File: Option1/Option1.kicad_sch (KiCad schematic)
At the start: 0 parts

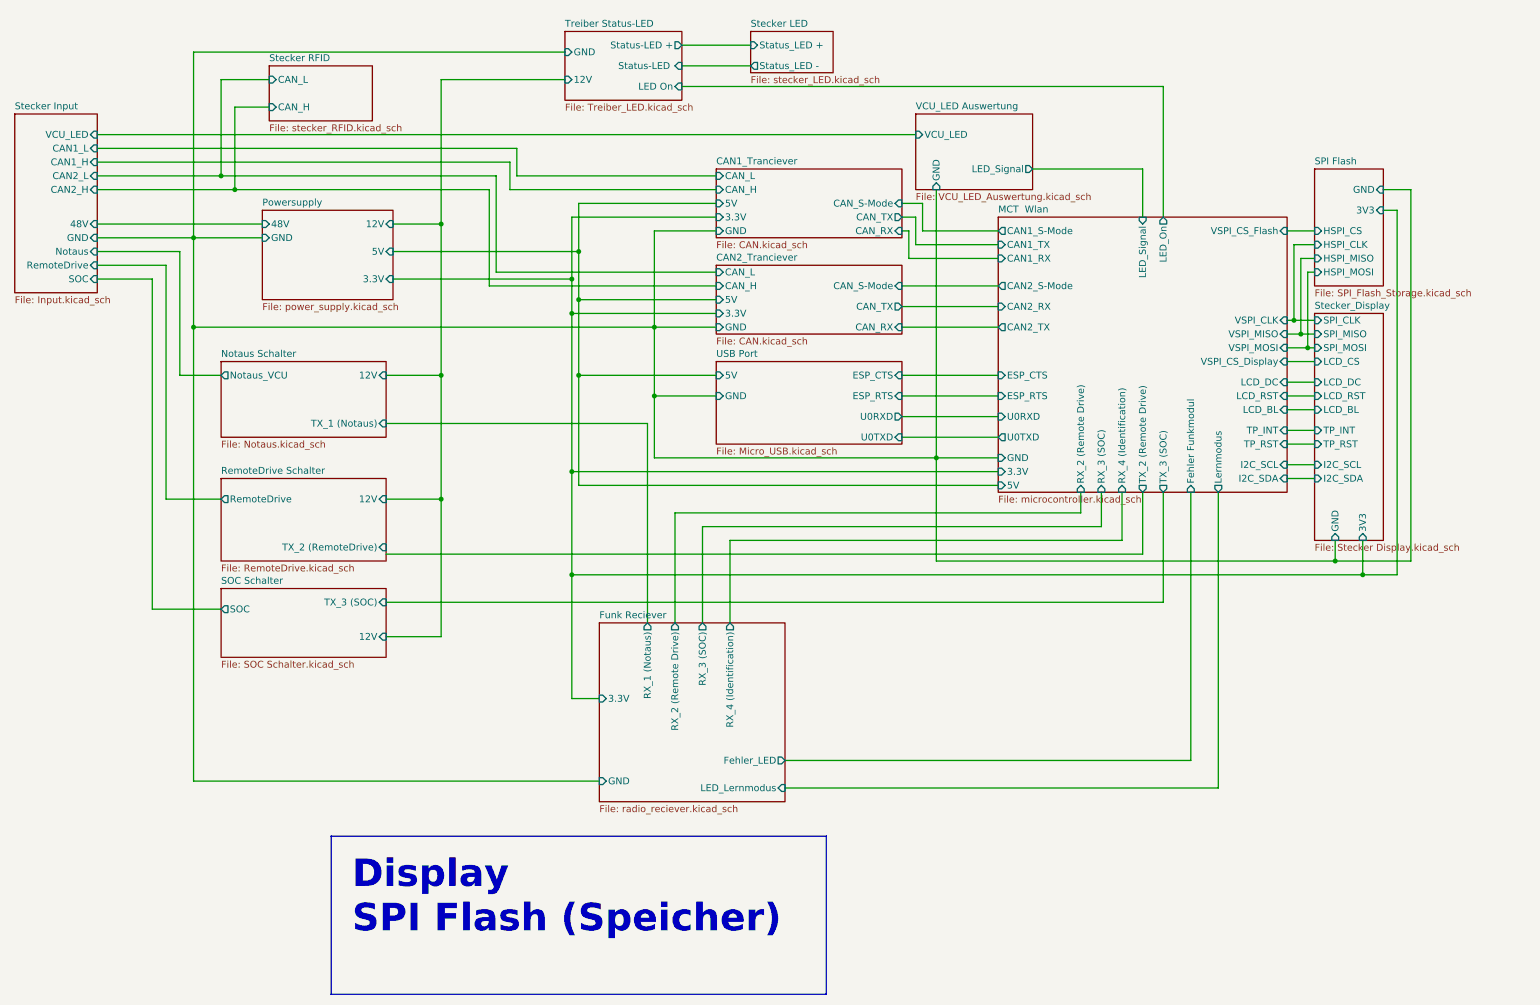
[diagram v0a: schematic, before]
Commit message: SPI Flash hinzugefügt, IN/Outputs vereinheitlicht, USB Flash Möglichkeit hinzugefügt, Display fehtl noch
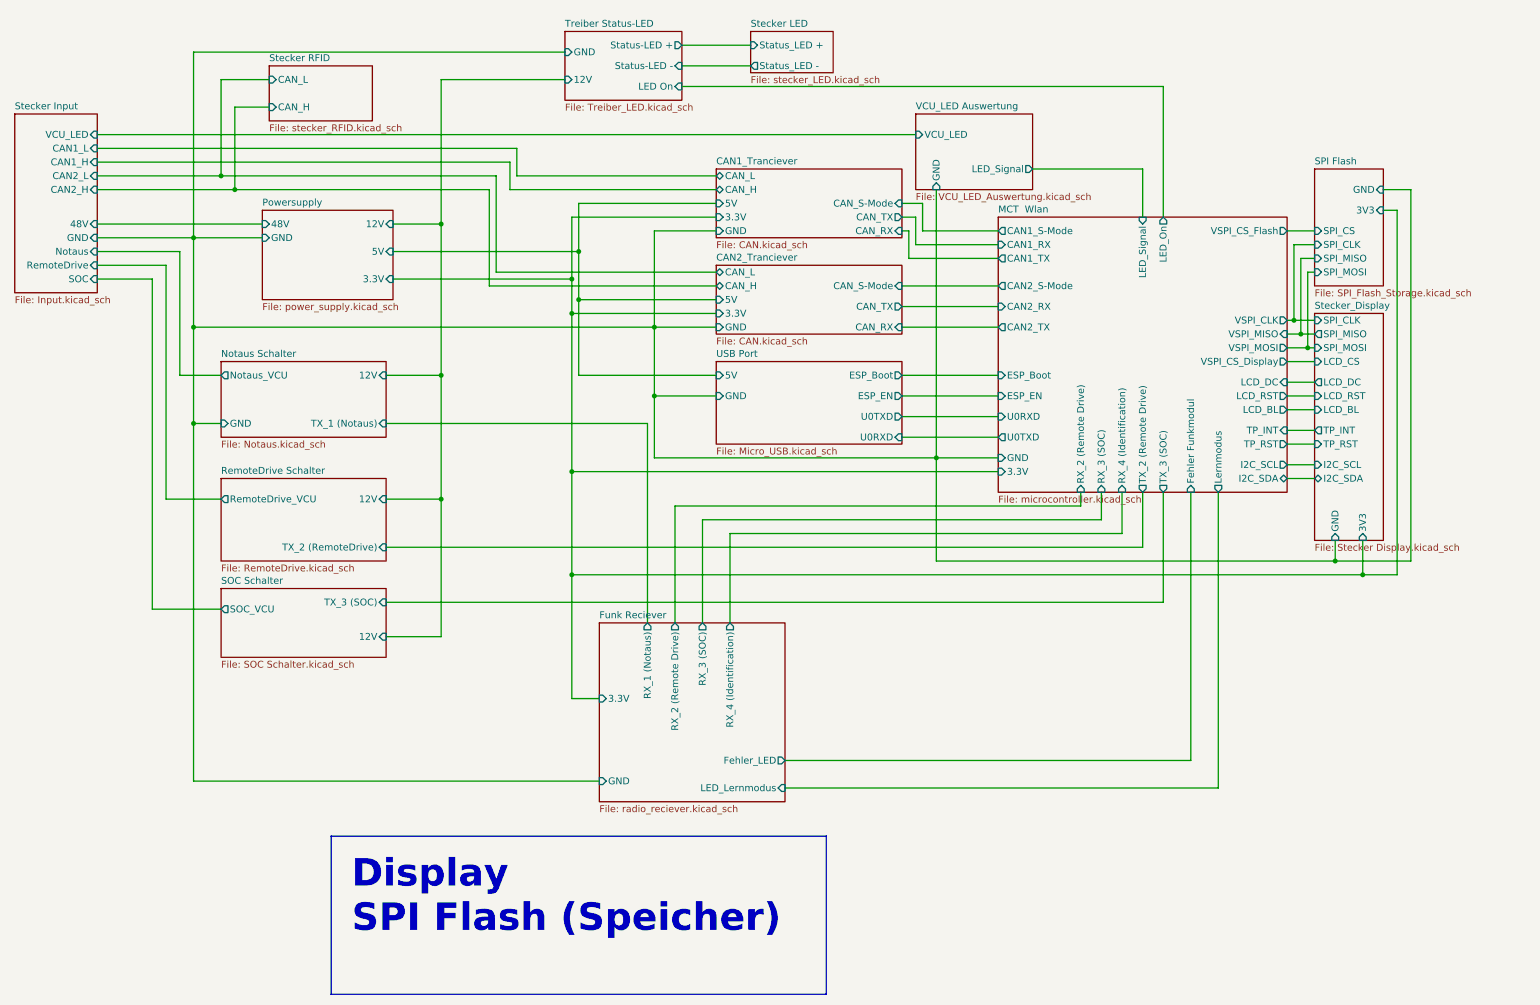
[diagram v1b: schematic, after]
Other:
- sheet MCT  Wlan ports: added ESP_Boot, ESP_EN; removed 5V, ESP_CTS, ESP_RTS
- sheet Notaus Schalter ports: added GND; removed none
- sheet RemoteDrive Schalter ports: added RemoteDrive_VCU; removed RemoteDrive
- sheet SOC Schalter ports: added SOC_VCU; removed SOC
- sheet SPI Flash ports: added SPI_CLK, SPI_CS, SPI_MISO, SPI_MOSI; removed HSPI_CLK, HSPI_CS, HSPI_MISO, HSPI_MOSI
- sheet Treiber Status-LED ports: added Status-LED -; removed Status-LED 
- sheet USB Port ports: added ESP_Boot, ESP_EN; removed ESP_CTS, ESP_RTS

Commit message: Added Export for Review 1
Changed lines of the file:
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@@
 		(comment 3 "Sebastian Hampl")
-	)
-	(text_box "Display\nSPI Flash (Speicher)\n"
-		(exclude_from_sim no)
-		(at 82.55 166.37 0)
-		(size 91.44 29.21)
-		(margins 3.81 3.81 3.81 3.81)
-		(stroke
-			(width 0)
-			(type default)
-		)
-		(fill
-			(type none)
-		)
-		(effects
-			(font
-				(size 5.08 5.08)
-				(thickness 1.016)
-				(bold yes)
-			)
-			(justify left top)
-		)
 	)
 	(junction

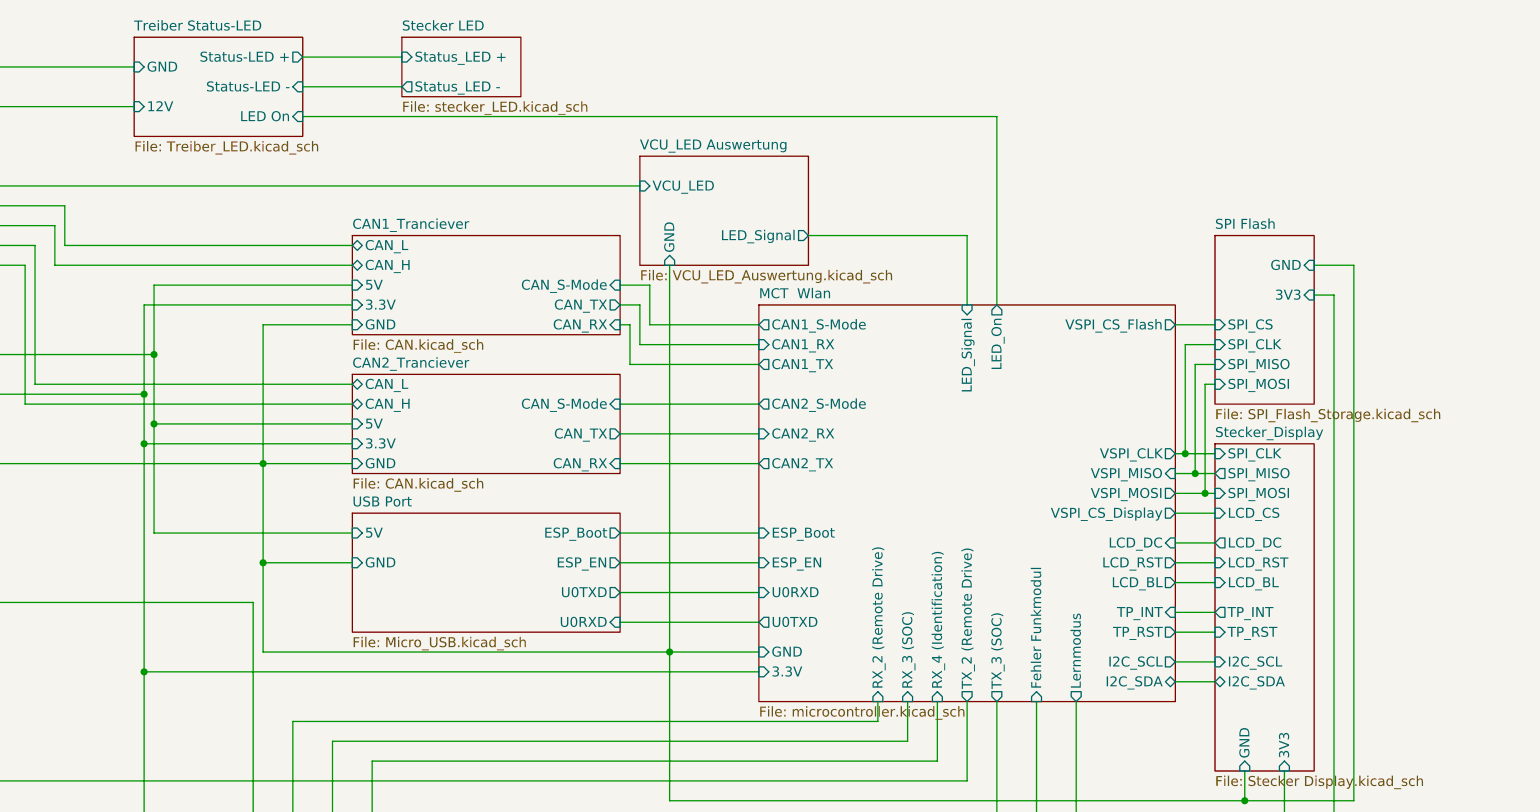
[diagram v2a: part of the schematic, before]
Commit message: USB auf 3V3 umgebaut
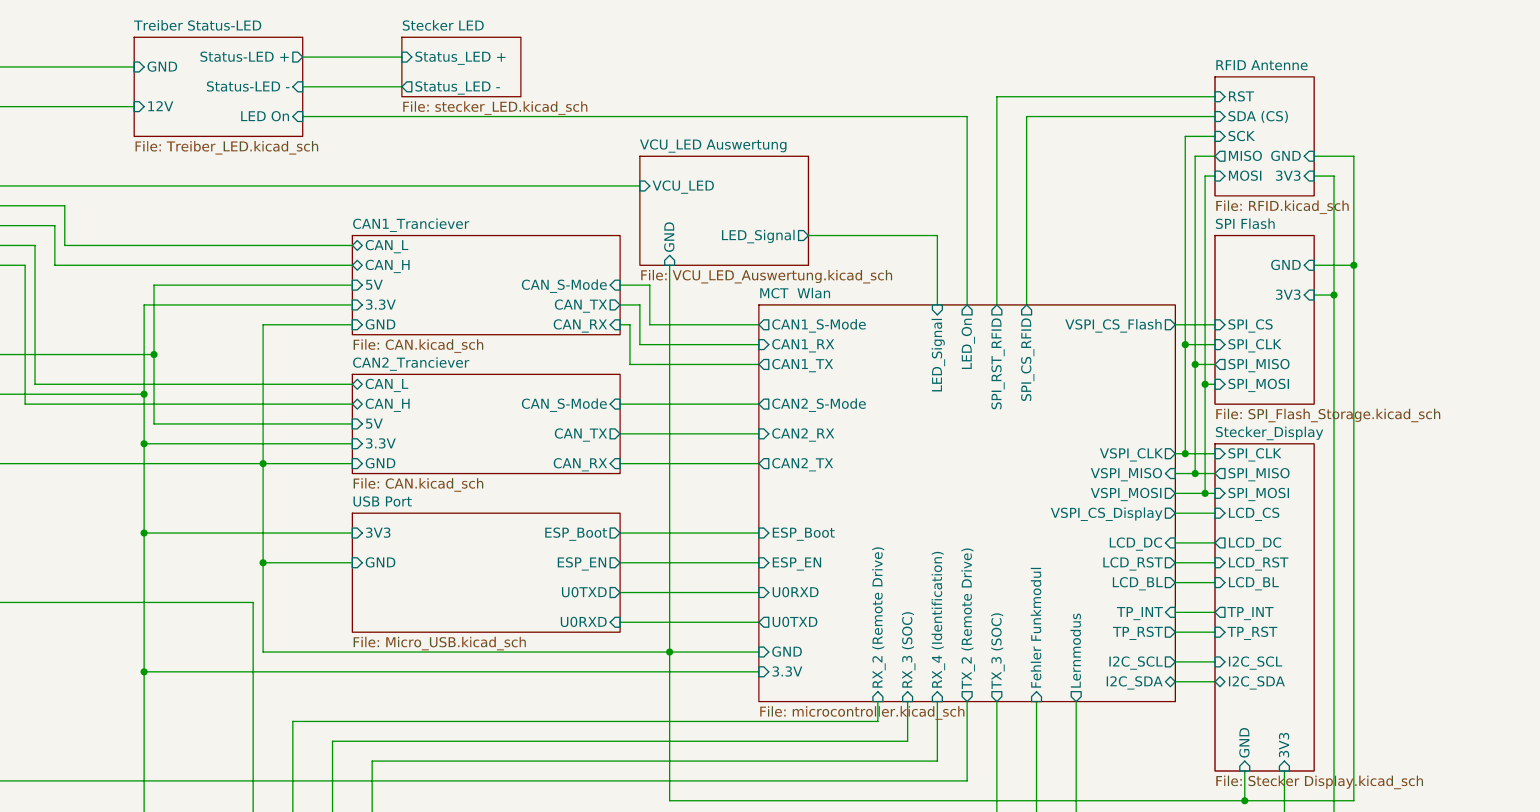
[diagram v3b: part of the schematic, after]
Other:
- added sheet RFID Antenne (RFID.kicad_sch)
- sheet MCT  Wlan ports: added SPI_CS_RFID, SPI_RST_RFID; removed none
- sheet USB Port ports: added 3V3; removed 5V

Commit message: Erste issues eingearbeitet
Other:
- removed sheet CAN1_Tranciever
- added sheet CAN1 Tranciever (CAN1.kicad_sch)
- sheet CAN2_Tranciever ports: added 3V3, SPI_CLK_CAN, SPI_CS_CAN, SPI_INT_CAN, SPI_MISO_CAN, SPI_MOSI_CAN; removed 3.3V, CAN_RX, CAN_TX
- sheet MCT  Wlan ports: added SPI_RST_CAN2, VSPI_CS_CAN2; removed CAN2_RX, CAN2_TX

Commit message: Pojekt und Backups
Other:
- sheet MCT  Wlan ports: added SPI_INT_CAN2; removed SPI_RST_CAN2
- sheet Powersupply ports: added 3.3V_D; removed none
- sheet RemoteDrive Schalter ports: added GND; removed none
- sheet SOC Schalter ports: added GND; removed none
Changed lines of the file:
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@@
 	)
 	(junction
-		(at 127 63.5)
-		(diameter 0)
-		(color 255 137 135 1)
-	)
-	(junction
 		(at 261.62 48.26)
 		(diameter 0)
@@
 	)
 	(junction
+		(at 57.15 113.03)
+		(diameter 0)
+		(color 0 0 0 0)
+	)
+	(junction
 		(at 127 73.66)
 		(diameter 0)
@@
 	)
 	(junction
+		(at 127 62.23)
+		(diameter 0)
+		(color 0 0 0 0)
+	)
+	(junction
 		(at 194.31 99.06)
 		(diameter 0)
@@
 	)
 	(junction
+		(at 57.15 129.54)
+		(diameter 0)
+		(color 0 0 0 0)
+	)
+	(junction
 		(at 102.87 81.28)
 		(diameter 0)
@@
 		(color 0 0 255 1)
 	)
-	(junction
-		(at 273.05 118.11)
-		(diameter 0)
-		(color 255 137 135 1)
-	)
 	(wire
 		(pts
@@
 	(wire
 		(pts
+			(xy 93.98 66.04) (xy 110.49 66.04)
+		)
+		(stroke
+			(width 0)
+			(type default)
+			(color 255 137 135 1)
+		)
+	)
+	(wire
+		(pts
 			(xy 127 83.82) (xy 127 101.6)
 		)
@@
 	(wire
 		(pts
-			(xy 93.98 63.5) (xy 127 63.5)
+			(xy 93.98 62.23) (xy 127 62.23)
 		)
 		(stroke
@@
 	(wire
 		(pts
-			(xy 127 52.07) (xy 127 63.5)
+			(xy 127 52.07) (xy 127 62.23)
 		)
 		(stroke
@@
 	(wire
 		(pts
-			(xy 57.15 90.17) (xy 57.15 156.21)
+			(xy 57.15 90.17) (xy 57.15 113.03)
 		)
 		(stroke
@@
 	(wire
 		(pts
+			(xy 57.15 113.03) (xy 62.23 113.03)
+		)
+		(stroke
+			(width 0.5)
+			(type default)
+			(color 0 0 0 1)
+		)
+	)
+	(wire
+		(pts
 			(xy 264.16 59.69) (xy 261.62 59.69)
 		)
@@
 	(wire
 		(pts
+			(xy 110.49 120.65) (xy 273.05 120.65)
+		)
+		(stroke
+			(width 0)
+			(type default)
+			(color 255 137 135 1)
+		)
+	)
+	(wire
+		(pts
 			(xy 194.31 40.64) (xy 198.12 40.64)
 		)
@@
 	(wire
 		(pts
+			(xy 127 62.23) (xy 127 73.66)
+		)
+		(stroke
+			(width 0)
+			(type default)
+			(color 255 137 135 1)
+		)
+	)
+	(wire
+		(pts
 			(xy 223.52 36.83) (xy 228.6 36.83)
 		)
@@
 	(wire
 		(pts
-			(xy 127 63.5) (xy 127 73.66)
-		)
-		(stroke
-			(width 0)
-			(type default)
-			(color 255 137 135 1)
-		)
-	)
-	(wire
-		(pts
 			(xy 166.37 157.48) (xy 246.38 157.48)
 		)
@@
 	(wire
 		(pts
+			(xy 57.15 113.03) (xy 57.15 129.54)
+		)
+		(stroke
+			(width 0.5)
+			(type default)
+			(color 0 0 0 1)
+		)
+	)
+	(wire
+		(pts
 			(xy 259.08 73.66) (xy 261.62 73.66)
 		)
@@
 	(wire
 		(pts
-			(xy 127 118.11) (xy 273.05 118.11)
+			(xy 127 118.11) (xy 279.4 118.11)
 		)
 		(stroke
@@
 	(wire
 		(pts
+			(xy 57.15 129.54) (xy 62.23 129.54)
+		)
+		(stroke
+			(width 0.5)
+			(type default)
+			(color 0 0 0 1)
+		)
+	)
+	(wire
+		(pts
 			(xy 259.08 93.98) (xy 264.16 93.98)
 		)
@@
 	(wire
 		(pts
-			(xy 220.98 102.87) (xy 220.98 105.41)
+			(xy 273.05 120.65) (xy 273.05 111.76)
 		)
 		(stroke
 			(width 0)
 			(type default)
+			(color 255 137 135 1)
 		)
 	)
 	(wire
 		(pts
-			(xy 187.96 95.25) (xy 205.74 95.25)
+			(xy 110.49 66.04) (xy 110.49 120.65)
 		)
 		(stroke
 			(width 0)
 			(type default)
+			(color 255 137 135 1)
 		)
 	)
 	(wire
 		(pts
-			(xy 259.08 54.61) (xy 264.16 54.61)
+			(xy 220.98 102.87) (xy 220.98 105.41)
 		)
 		(stroke
@@
 	(wire
 		(pts
-			(xy 224.79 102.87) (xy 224.79 107.95)
+			(xy 187.96 95.25) (xy 205.74 95.25)
 		)
 		(stroke
@@
 	(wire
 		(pts
-			(xy 92.71 104.14) (xy 102.87 104.14)
+			(xy 259.08 54.61) (xy 264.16 54.61)
 		)
 		(stroke
-			(width 0.5)
+			(width 0)
 			(type default)
-			(color 255 0 4 1)
 		)
 	)
 	(wire
 		(pts
-			(xy 236.22 52.07) (xy 236.22 25.4)
+			(xy 224.79 102.87) (xy 224.79 107.95)
 		)
 		(stroke
@@
 	(wire
 		(pts
-			(xy 273.05 118.11) (xy 279.4 118.11)
+			(xy 92.71 104.14) (xy 102.87 104.14)
 		)
 		(stroke
-			(width 0)
+			(width 0.5)
 			(type default)
-			(color 255 137 135 1)
+			(color 255 0 4 1)
 		)
 	)
 	(wire
 		(pts
-			(xy 259.08 71.12) (xy 260.35 71.12)
+			(xy 236.22 52.07) (xy 236.22 25.4)
 		)
 		(stroke
@@
 	(wire
 		(pts
-			(xy 273.05 111.76) (xy 273.05 118.11)
+			(xy 259.08 71.12) (xy 260.35 71.12)
 		)
 		(stroke
 			(width 0)
 			(type default)
-			(color 255 137 135 1)
 		)
 	)
@@
 	(wire
 		(pts
+			(xy 57.15 129.54) (xy 57.15 156.21)
+		)
+		(stroke
+			(width 0.5)
+			(type default)
+			(color 0 0 0 1)
+		)
+	)
+	(wire
+		(pts
 			(xy 261.62 48.26) (xy 261.62 59.69)
 		)
@@
 			)
 		)
+		(pin "GND" input
+			(at 62.23 129.54 180)
+			(effects
+				(font
+					(size 1.27 1.27)
+				)
+				(justify left)
+			)
+		)
 		(instances
 			(project "Option1"
@@
 			)
 		)
-		(pin "SPI_RST_CAN2" output
+		(pin "SPI_INT_CAN2" input
 			(at 205.74 53.34 180)
 			(effects
@@
 			)
 		)
+		(pin "GND" input
+			(at 62.23 113.03 180)
+			(effects
+				(font
+					(size 1.27 1.27)
+				)
+				(justify left)
+			)
+		)
 		(instances
 			(project "Option1"
@@
 		)
 		(pin "3.3V" input
-			(at 93.98 63.5 0)
+			(at 93.98 62.23 0)
+			(effects
+				(font
+					(size 1.27 1.27)
+				)
+				(justify right)
+			)
+		)
+		(pin "3.3V_D" input
+			(at 93.98 66.04 0)
 			(effects
 				(font
